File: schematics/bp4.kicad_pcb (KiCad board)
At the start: 2 copper layers, 90 x 30 mm, 29 parts, among them J1 Left Pin Strip, J2 Right Pin Strip, J3 I/O Pin Strip, J4 Power Pins A, J5 Power Pins B, J6 Power Pins C, SW1 Power Switch, U1 TPS61220DCK, U2 LM321

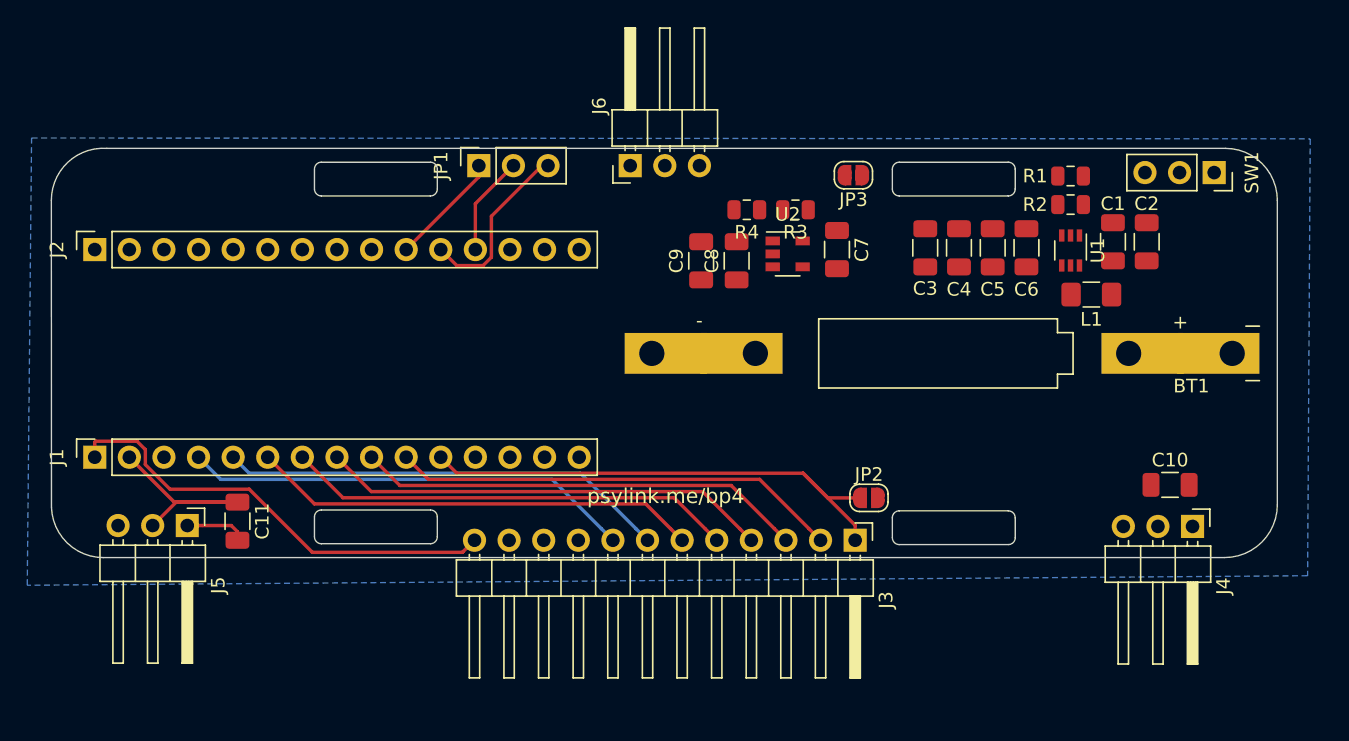
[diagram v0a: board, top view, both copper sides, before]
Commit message: added circuit 11 and small changes to bp4
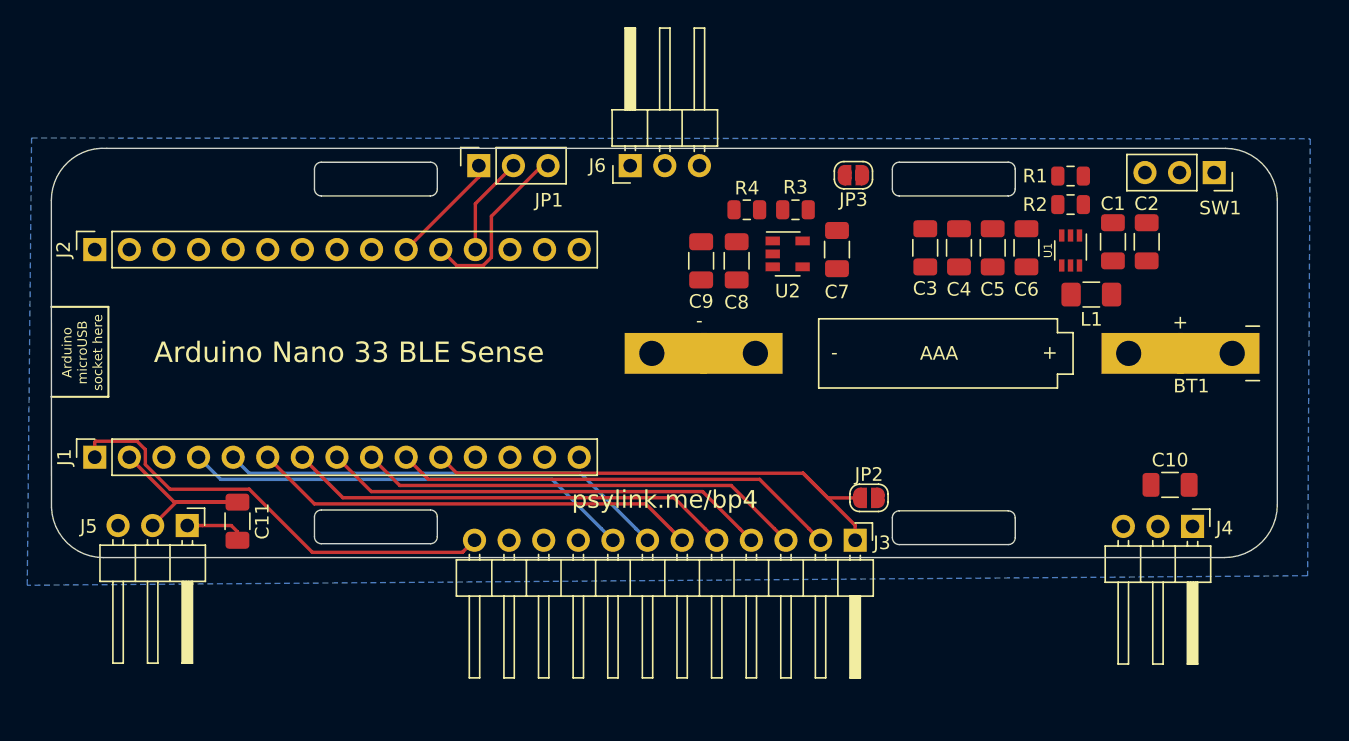
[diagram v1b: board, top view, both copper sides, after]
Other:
- board text added: "+"
- board text added: "-"
- board text added: "AAA"
- board text added: "Arduino Nano 33 BLE Sense"
- board text added: "Arduino microUSB socket here"
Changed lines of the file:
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@@
   (general
     (thickness 1.6)
-    (drawings 49)
+    (drawings 57)
     (tracks 63)
     (zones 0)
@@
     (tags capacitor)
     (attr smd)
-    (fp_text reference C7 (at 0 -1.82 90) (layer F.SilkS)
+    (fp_text reference C7 (at 3.1115 0 180) (layer F.SilkS)
       (effects (font (size 1 1) (thickness 0.15)))
     )
@@
     (tags capacitor)
     (attr smd)
-    (fp_text reference C8 (at 0 -1.82 90) (layer F.SilkS)
+    (fp_text reference C8 (at -3.048 0 180) (layer F.SilkS)
       (effects (font (size 1 1) (thickness 0.15)))
     )
@@
     (tags capacitor)
     (attr smd)
-    (fp_text reference C9 (at 0 -1.82 90) (layer F.SilkS)
+    (fp_text reference C9 (at -2.9845 0 180) (layer F.SilkS)
       (effects (font (size 1 1) (thickness 0.15)))
     )
@@
     (descr "Through hole straight socket strip, 1x15, 2.54mm pitch, single row (from Kicad 4.0.7), script generated")
     (tags "Through hole socket strip THT 1x15 2.54mm single row")
-    (fp_text reference J1 (at 0 -2.77 90) (layer F.SilkS)
+    (fp_text reference J1 (at 0 -2.2225 90) (layer F.SilkS)
       (effects (font (size 1 1) (thickness 0.15)))
     )
@@
     (descr "Through hole straight socket strip, 1x15, 2.54mm pitch, single row (from Kicad 4.0.7), script generated")
     (tags "Through hole socket strip THT 1x15 2.54mm single row")
-    (fp_text reference J2 (at 0 -2.77 90) (layer F.SilkS)
+    (fp_text reference J2 (at 0 -2.286 90) (layer F.SilkS)
       (effects (font (size 1 1) (thickness 0.15)))
     )
@@
     (descr "Through hole straight socket strip, 1x03, 2.54mm pitch, single row (from Kicad 4.0.7), script generated")
     (tags "Through hole socket strip THT 1x03 2.54mm single row")
-    (fp_text reference JP1 (at 0 -2.77 90) (layer F.SilkS)
+    (fp_text reference JP1 (at -2.54 5.1435 180) (layer F.SilkS)
       (effects (font (size 1 1) (thickness 0.15)))
     )
@@
     (tags resistor)
     (attr smd)
-    (fp_text reference R3 (at 0 -1.65) (layer F.SilkS)
+    (fp_text reference R3 (at 0 1.651) (layer F.SilkS)
       (effects (font (size 1 1) (thickness 0.15)))
     )
@@
     (tags resistor)
     (attr smd)
-    (fp_text reference R4 (at 0 -1.65) (layer F.SilkS)
+    (fp_text reference R4 (at -0.015 1.5875) (layer F.SilkS)
       (effects (font (size 1 1) (thickness 0.15)))
     )
@@
     (descr "Through hole straight socket strip, 1x03, 2.54mm pitch, single row (from Kicad 4.0.7), script generated")
     (tags "Through hole socket strip THT 1x03 2.54mm single row")
-    (fp_text reference SW1 (at 0 -2.77 90) (layer F.SilkS)
+    (fp_text reference SW1 (at 2.6035 -0.4445 180) (layer F.SilkS)
       (effects (font (size 1 1) (thickness 0.15)))
     )
@@
     (tags "R-PDSO-G6 SC-70-6")
     (attr smd)
-    (fp_text reference U1 (at 0 -2 90) (layer F.SilkS)
-      (effects (font (size 1 1) (thickness 0.15)))
+    (fp_text reference U1 (at 0 1.651 270) (layer F.SilkS)
+      (effects (font (size 0.6 0.6) (thickness 0.1)))
     )
     (fp_text value TPS61220DCK (at 0 2 90) (layer F.Fab)
@@
     (tags SOT-23-5)
     (attr smd)
-    (fp_text reference U2 (at 0 -2.9) (layer F.SilkS)
+    (fp_text reference U2 (at 0 2.7305) (layer F.SilkS)
       (effects (font (size 1 1) (thickness 0.15)))
     )
@@
     (descr "Through hole angled pin header, 1x12, 2.54mm pitch, 6mm pin length, single row")
     (tags "Through hole angled pin header THT 1x12 2.54mm single row")
-    (fp_text reference J3 (at 4.385 -2.27 90) (layer F.SilkS)
+    (fp_text reference J3 (at 0.1905 -1.9685 180) (layer F.SilkS)
       (effects (font (size 1 1) (thickness 0.15)))
     )
@@
     (descr "Through hole angled pin header, 1x03, 2.54mm pitch, 6mm pin length, single row")
     (tags "Through hole angled pin header THT 1x03 2.54mm single row")
-    (fp_text reference J4 (at 4.385 -2.27 90) (layer F.SilkS)
+    (fp_text reference J4 (at 0.127 -2.3495 180) (layer F.SilkS)
       (effects (font (size 1 1) (thickness 0.15)))
     )
@@
     (descr "Through hole angled pin header, 1x03, 2.54mm pitch, 6mm pin length, single row")
     (tags "Through hole angled pin header THT 1x03 2.54mm single row")
-    (fp_text reference J5 (at 4.385 -2.27 90) (layer F.SilkS)
+    (fp_text reference J5 (at 0.0635 7.239 180) (layer F.SilkS)
       (effects (font (size 1 1) (thickness 0.15)))
     )
@@
     (descr "Through hole angled pin header, 1x03, 2.54mm pitch, 6mm pin length, single row")
     (tags "Through hole angled pin header THT 1x03 2.54mm single row")
-    (fp_text reference J6 (at 4.385 -2.27 90) (layer F.SilkS)
+    (fp_text reference J6 (at 0 -2.413 180) (layer F.SilkS)
       (effects (font (size 1 1) (thickness 0.15)))
     )
@@
     )
   )
+  (gr_text + (at 98.679 40.386) (layer F.SilkS)
+    (effects (font (size 1 1) (thickness 0.15)))
+  )
+  (gr_text - (at 82.8675 40.386) (layer F.SilkS)
+    (effects (font (size 1 1) (thickness 0.15)))
+  )
+  (gr_text AAA (at 90.551 40.4495) (layer F.SilkS)
+    (effects (font (size 1 1) (thickness 0.15)))
+  )
+  (gr_text "Arduino Nano 33 BLE Sense" (at 47.244 40.386) (layer F.SilkS)
+    (effects (font (size 1.5 1.5) (thickness 0.3)))
+  )
+  (gr_line (start 25.3873 37.0332) (end 29.5783 37.0332) (layer F.SilkS) (width 0.15))
+  (gr_line (start 29.5783 37.0332) (end 29.5783 43.6372) (layer F.SilkS) (width 0.15))
+  (gr_line (start 29.5783 43.6372) (end 25.3873 43.6372) (layer F.SilkS) (width 0.15))
+  (gr_text "Arduino\nmicroUSB\nsocket here" (at 27.6733 40.386 90) (layer F.SilkS)
+    (effects (font (size 0.7 0.7) (thickness 0.12)))
+  )
   (gr_line (start 66.8655 34.6075) (end 114.681 34.6075) (layer Dwgs.User) (width 0.15))
   (gr_line (start 66.8655 46.228) (end 114.681 46.228) (layer Dwgs.User) (width 0.15))
@@
   (gr_line (start 25.4 55.4355) (end 115.3795 55.4355) (layer Dwgs.User) (width 0.15))
   (gr_line (start 25.4 25.4) (end 115.3795 25.4) (layer Dwgs.User) (width 0.15))
-  (gr_text psylink.me/bp4 (at 70.485 50.927) (layer F.SilkS)
-    (effects (font (size 1.1 1.1) (thickness 0.2)))
+  (gr_text psylink.me/bp4 (at 70.4215 51.181) (layer F.SilkS)
+    (effects (font (size 1.3 1.3) (thickness 0.2)))
   )
   (gr_arc (start 53.213 28.3845) (end 53.213 28.8925) (angle -90) (layer Edge.Cuts) (width 0.1))

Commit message: WIP bp4
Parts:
- added EL5: Electrode, MountingHole:MountingHole_3.7mm_Pad, F.Cu at (111.3, 29.5)
- added EL5: Electrode, MountingHole:MountingHole_3.7mm_Pad, F.Cu at (111.3, 53.9)
- added EL5: Electrode, MountingHole:MountingHole_3.7mm_Pad, F.Cu at (29.5, 29.5)
- added EL5: Electrode, MountingHole:MountingHole_3.7mm_Pad, F.Cu at (29.5, 54.0)
- added REF_ELECTRODE: Electrode, MountingHole:MountingHole_3.7mm_Pad, F.Cu at (61.3, 41.8)
- moved C3 21.7 mm to (67.8, 33.4)
- moved C2 16.3 mm to (89.6, 34.1), turned to 90 degrees
- moved R1 12.5 mm to (95.2, 38.9), turned to 180 degrees
- moved C4 11.4 mm to (103.4, 33.7), turned to 270 degrees
- moved C1 11.4 mm to (92.1, 34.1), turned to 90 degrees
- moved L1 10.00 mm to (93.7, 30.2), turned to 0 degrees
- moved R2 8.86 mm to (95.2, 36.8), turned to 0 degrees
- moved C5 6.48 mm to (100.9, 33.7), turned to 270 degrees
- moved J5 6.22 mm to (40.4, 56.8)
- moved C10 6.13 mm to (102.6, 53.7)
- moved J4 6.13 mm to (104.2, 56.8)
- moved U1 5.05 mm to (95.2, 33.5), turned to 90 degrees
- moved C11 3.23 mm to (36.0, 53.8), turned to 0 degrees
- moved J3 2.60 mm to (84.4, 56.8)
- moved SW1 2.34 mm to (108.5, 26.7)
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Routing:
- net /V+: track 16.2 -> 84.4 mm
- net /GND: track 11.8 -> 30.6 mm, vias 0 -> 2
- net /Vbat: track 0.00 -> 12.3 mm, vias 0 -> 2
- net /OpAmpV+: track 0.00 -> 9.32 mm
- net /Vref: track 0.00 -> 7.85 mm
- net /D13: track 33.4 -> 39.6 mm, vias 0 -> 2
- net /Vdiv: track 0.00 -> 3.98 mm
- net /A7: track 38.5 -> 35.9 mm
- net /A6: track 32.9 -> 35.3 mm
- net /A5: track 32.9 -> 35.3 mm
- net /A4: track 32.9 -> 35.3 mm
- net /A2: track 32.9 -> 35.3 mm
- net /A0: track 32.9 -> 35.3 mm
- net /A3: track 32.9 -> 35.3 mm
- net /A1: track 32.9 -> 35.3 mm
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- added copper zone on B.Cu, net /GND
- added copper zone on F.Cu, net /GND
- added copper zone on F.Cu, net /L
- added copper zone on F.Cu, net /V+
- removed copper zone on B.Cu, net Earth
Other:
- board size 90 x 30 mm -> 90 x 32.6 mm
- board text added: "L1 is super noisy, keep other components away from it!"

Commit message: routed bp4, jumpers & labels missing tho
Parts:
- C1, C10, C11, C2, C3, C4, C5, C6, C7, C8, C9: footprint Capacitor_SMD:C_1206_3216Metric -> Capacitor_SMD:C_1206_3216Metric_Pad1.42x1.75mm_HandSolder
- J4, J5: moved to B.Cu
- L1: footprint Inductor_SMD:L_1206_3216Metric_Pad1.42x1.75mm_HandSolder -> Inductor_SMD:L_1210_3225Metric_Pad1.42x2.65mm_HandSolder
- R1, R2, R3, R4: footprint Resistor_SMD:R_0805_2012Metric -> Resistor_SMD:R_0805_2012Metric_Pad1.15x1.40mm_HandSolder
- moved C6 30.6 mm to (67.8, 33.3), turned to 90 degrees
- moved C3 29.8 mm to (97.6, 34.9), turned to 270 degrees
- moved C11 11.0 mm to (28.4, 45.9), turned to 180 degrees
- moved J5 5.14 mm to (35.2, 56.7)
- moved J4 3.68 mm to (100.5, 56.8)
- moved C1 3.52 mm to (88.8, 35.3)
- moved C4 3.46 mm to (100.1, 34.9)
- moved SW1 3.05 mm to (105.4, 26.7)
- moved C8 2.73 mm to (73.3, 33.4)
- moved C9 2.35 mm to (75.8, 33.4)
- moved C5 2.15 mm to (102.7, 34.9)
- moved C2 2.04 mm to (91.2, 35.3)
- moved JP2 1.86 mm to (84.9, 52.8)
- moved R1 1.46 mm to (94.4, 40.1)
- moved R2 1.46 mm to (94.4, 38.0)
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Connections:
- REF_ELECTRODE pad 1: (no net) -> /Vref
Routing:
- net /Vref: track 7.85 -> 147.5 mm, vias 0 -> 6
- net /V+: track 84.4 -> 177.8 mm, vias 0 -> 3
- net /D12: track 0.00 -> 61.1 mm, vias 0 -> 1
- net /D11: track 0.00 -> 59.2 mm, vias 0 -> 1
- net /D10: track 0.00 -> 57.6 mm, vias 0 -> 1
- net /Vbat: track 12.3 -> 59.0 mm, vias 2 -> 4
- net Net-(BT1-Pad1): track 0.00 -> 26.4 mm
- net /FB: track 0.00 -> 4.63 mm
- net /GND: track 30.6 -> 33.6 mm, vias 2 -> 4
- net /D13: track 39.6 -> 37.0 mm
- net /A7: track 35.9 -> 38.0 mm
- net /D2: track 12.7 -> 13.8 mm
- net /Vdiv: track 3.98 -> 4.61 mm
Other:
- board text added: "AAA Battery"
- board text removed: "AAA"

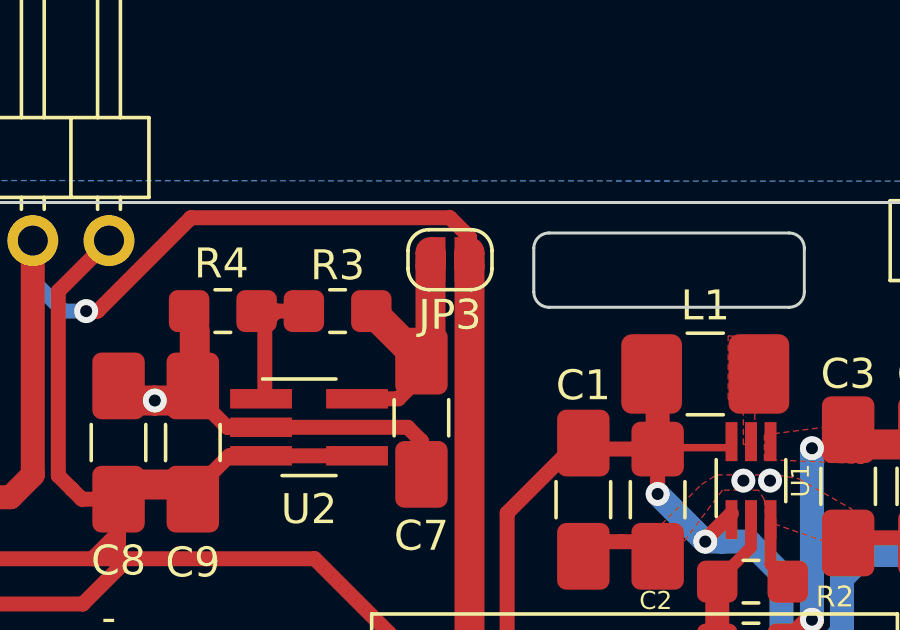
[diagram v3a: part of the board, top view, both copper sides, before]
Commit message: added screws & solder jumpers to circuit11
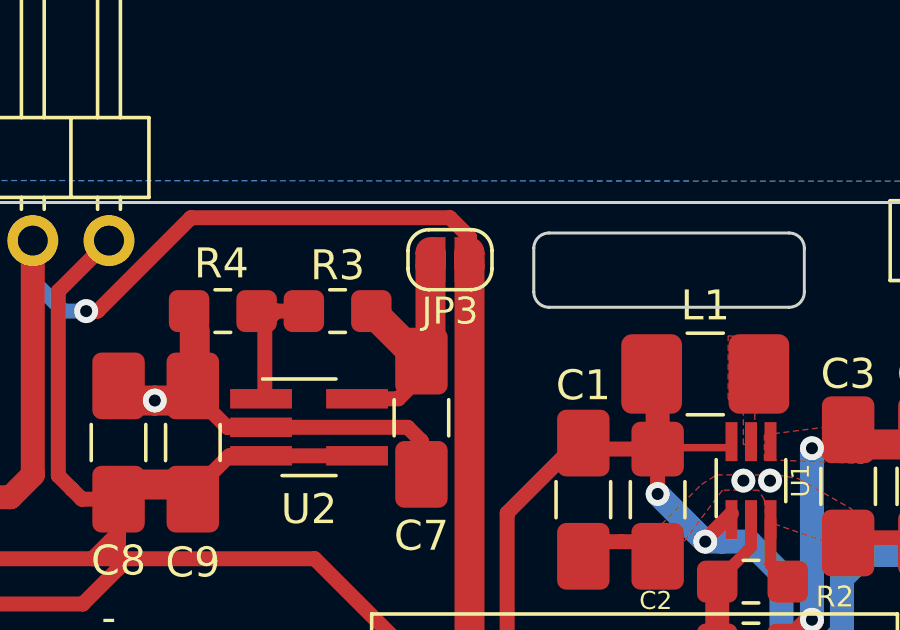
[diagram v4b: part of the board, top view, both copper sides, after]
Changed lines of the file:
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@@
     (tags "solder jumper open")
     (attr virtual)
-    (fp_text reference JP3 (at 0 -1.8415) (layer F.SilkS)
-      (effects (font (size 1 1) (thickness 0.15)))
+    (fp_text reference JP3 (at 0 -1.7145) (layer F.SilkS)
+      (effects (font (size 0.9 0.9) (thickness 0.15)))
     )
     (fp_text value "Solder Jumper" (at 0 1.9) (layer F.Fab)

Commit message: finished bp4 (or so it seems)
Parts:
- removed EL5 (x4), REF_ELECTRODE: Electrode, MountingHole:MountingHole_3.7mm_Pad
- added JP4: SolderJumper_2_Open, Jumper:SolderJumper-2_P1.3mm_Open_RoundedPad1.0x1.5mm, F.Cu at (36.3, 27.4)
- added JP5: SolderJumper_2_Open, Jumper:SolderJumper-2_P1.3mm_Open_RoundedPad1.0x1.5mm, F.Cu at (112.8, 34.7)
- added JP6: SolderJumper_2_Open, Jumper:SolderJumper-2_P1.3mm_Open_RoundedPad1.0x1.5mm, F.Cu at (35.3, 53.7)
- added JP7: SolderJumper_2_Open, Jumper:SolderJumper-2_P1.3mm_Open_RoundedPad1.0x1.5mm, F.Cu at (106.2, 49.5)
- added JP8: SolderJumper_2_Open, Jumper:SolderJumper-2_P1.3mm_Open_RoundedPad1.0x1.5mm, F.Cu at (70.0, 38.5)
- added Screw1: Top Left, MountingHole:MountingHole_3.7mm_Pad, F.Cu at (29.5, 29.5)
- added Screw2: Top Right, MountingHole:MountingHole_3.7mm_Pad, F.Cu at (111.3, 29.5)
- added Screw3: Bottom Left, MountingHole:MountingHole_3.7mm_Pad, F.Cu at (29.5, 54.0)
- added Screw4: Bottom Right, MountingHole:MountingHole_3.7mm_Pad, F.Cu at (111.3, 53.9)
- added Screw5: Center, MountingHole:MountingHole_3.7mm_Pad, F.Cu at (61.3, 41.8)
- moved C10 0.51 mm to (101.6, 53.3)
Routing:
- net /Vref: track 147.5 -> 171.5 mm, vias 6 -> 8
- net Net-(JP8-Pad2): track 0.00 -> 9.39 mm
- net Net-(JP4-Pad2): track 0.00 -> 7.01 mm
- net Net-(JP7-Pad2): track 0.00 -> 6.24 mm
- net Net-(JP5-Pad2): track 0.00 -> 5.54 mm
- net Net-(JP6-Pad2): track 0.00 -> 5.28 mm
- net /V+: track 177.8 -> 180.1 mm
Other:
- board text added: "5V Boost Converter"
- board text added: "D13 D12 D11 D10 A0 A1 A2 A3 A4 A5 A6 A7"
- board text added: "GND V+ Vref"
- board text added: "Slot for Arduino Nano 33 BLE Sense"
- board text added: "Vbat track goes a weird way to avoid noisiness of L1"
- board text added: "Vref Generator"
- board text removed: "Arduino Nano 33 BLE Sense"
